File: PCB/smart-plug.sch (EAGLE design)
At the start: 10 parts, among them K1 HLS8L-DC3V-S-C, T1 2N2222

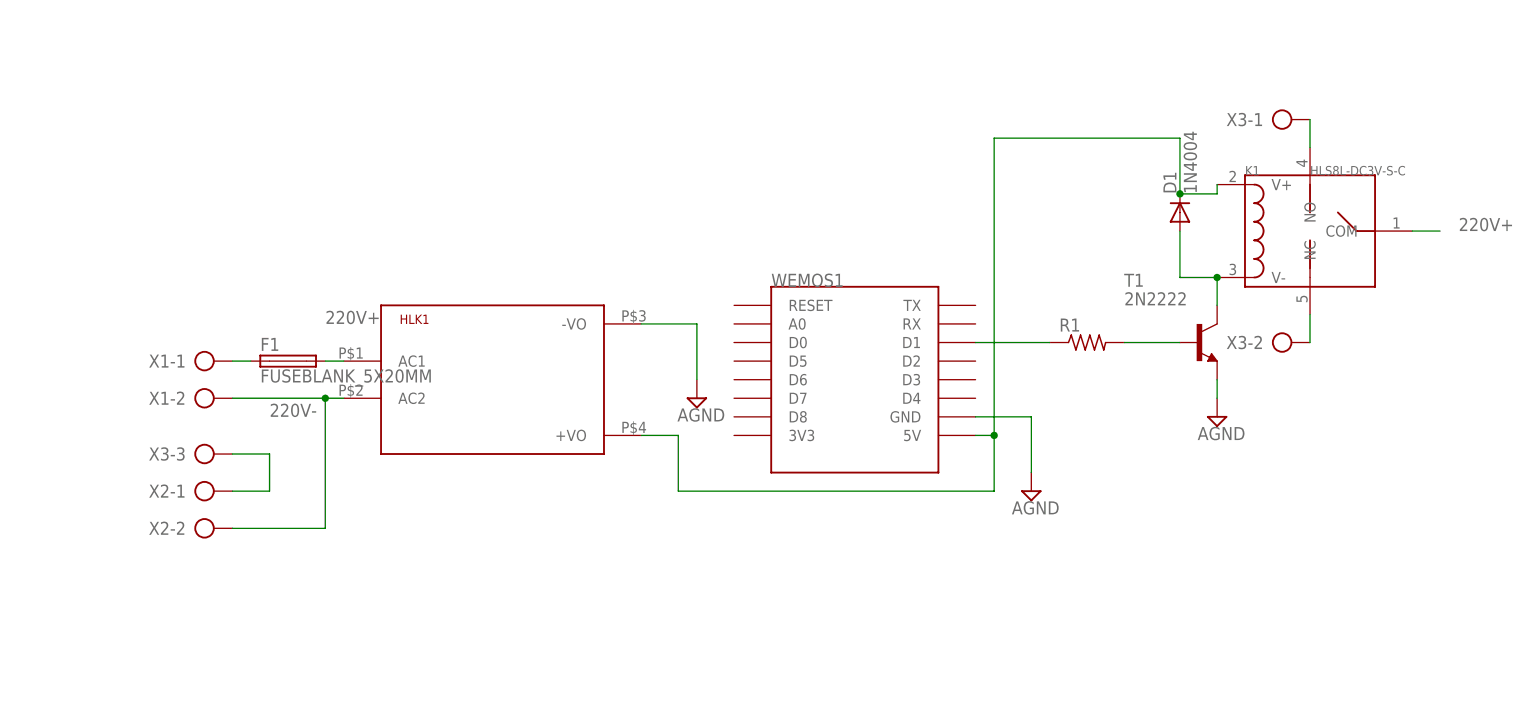
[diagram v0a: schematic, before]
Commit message: Update files
Added LED indicators
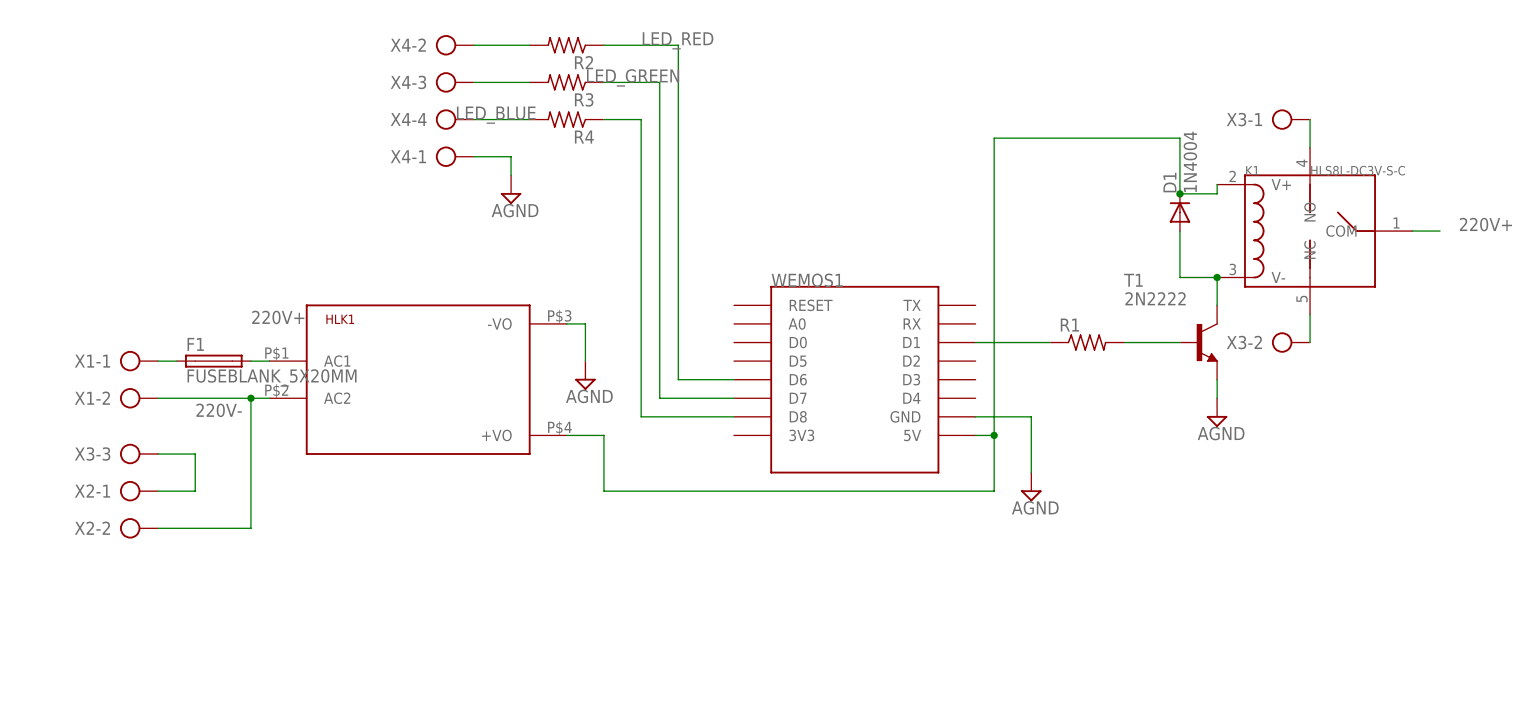
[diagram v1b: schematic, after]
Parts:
- added R2, R3, R4: (no value), adafruit:R-US_0207/10
- added X4: (no value), con-ptr500:AK300/4
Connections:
- new net LED_BLUE: R4.1, WEMOS1.D8
- new net LED_GREEN: R3.1, WEMOS1.D7
- new net LED_RED: R2.1, WEMOS1.D6
- new net N$10: R4.2, X4-4.KL
- new net N$11: R3.2, X4-3.KL
- new net N$9: R2.2, X4-2.KL
- net AGND: now also X4-1.KL
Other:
- moved on the sheet: F1, HLK1, X1-1, X1-2, X2-1, X2-2, X3-3
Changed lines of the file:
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@@
 <part name="F1" library="fuse" library_urn="urn:adsk.eagle:library:233" deviceset="FUSE" device="BLANK_5X20MM" package3d_urn="urn:adsk.eagle:package:14079/1"/>
 <part name="SUPPLY3" library="supply2" library_urn="urn:adsk.eagle:library:372" deviceset="AGND" device=""/>
+<part name="R2" library="adafruit" deviceset="R-US_" device="0207/10"/>
+<part name="R3" library="adafruit" deviceset="R-US_" device="0207/10"/>
+<part name="R4" library="adafruit" deviceset="R-US_" device="0207/10"/>
+<part name="X4" library="con-ptr500" library_urn="urn:adsk.eagle:library:181" deviceset="AK300/4" device="" package3d_urn="urn:adsk.eagle:package:9879/1"/>
+<part name="SUPPLY4" library="supply2" library_urn="urn:adsk.eagle:library:372" deviceset="AGND" device=""/>
 </parts>
 <sheets>
@@
 <instance part="SUPPLY2" gate="G$1" x="142.24" y="58.42"/>
 <instance part="D1" gate="1" x="137.16" y="86.36" rot="R90"/>
-<instance part="HLK1" gate="G$1" x="43.18" y="63.5"/>
-<instance part="X1" gate="-1" x="2.54" y="66.04"/>
-<instance part="X1" gate="-2" x="2.54" y="60.96"/>
-<instance part="X2" gate="-1" x="2.54" y="48.26"/>
-<instance part="X2" gate="-2" x="2.54" y="43.18"/>
+<instance part="HLK1" gate="G$1" x="33.02" y="63.5"/>
+<instance part="X1" gate="-1" x="-7.62" y="66.04"/>
+<instance part="X1" gate="-2" x="-7.62" y="60.96"/>
+<instance part="X2" gate="-1" x="-7.62" y="48.26"/>
+<instance part="X2" gate="-2" x="-7.62" y="43.18"/>
 <instance part="X3" gate="-1" x="149.86" y="99.06"/>
 <instance part="X3" gate="-2" x="149.86" y="68.58"/>
-<instance part="X3" gate="-3" x="2.54" y="53.34"/>
-<instance part="F1" gate="G$1" x="15.24" y="66.04"/>
-<instance part="SUPPLY3" gate="G$1" x="71.12" y="60.96"/>
+<instance part="X3" gate="-3" x="-7.62" y="53.34"/>
+<instance part="F1" gate="G$1" x="5.08" y="66.04"/>
+<instance part="SUPPLY3" gate="G$1" x="55.88" y="63.5"/>
+<instance part="R2" gate="G$1" x="53.34" y="109.22" rot="R180"/>
+<instance part="R3" gate="G$1" x="53.34" y="104.14" rot="R180"/>
+<instance part="R4" gate="G$1" x="53.34" y="99.06" rot="R180"/>
+<instance part="X4" gate="-1" x="35.56" y="93.98"/>
+<instance part="X4" gate="-2" x="35.56" y="109.22"/>
+<instance part="X4" gate="-3" x="35.56" y="104.14"/>
+<instance part="X4" gate="-4" x="35.56" y="99.06"/>
+<instance part="SUPPLY4" gate="G$1" x="45.72" y="88.9"/>
 </instances>
 <busses>
 </busses>
 <nets>
-<net name="N$2" class="0">
-<segment>
-<pinref part="WEMOS1" gate="D1" pin="D1"/>
-<pinref part="R1" gate="G$1" pin="1"/>
-<wire x1="109.22" y1="68.58" x2="119.38" y2="68.58" width="0.1524" layer="91"/>
-</segment>
-</net>
 <net name="N$3" class="0">
 <segment>
@@
 <wire x1="111.76" y1="55.88" x2="109.22" y2="55.88" width="0.1524" layer="91"/>
 <pinref part="HLK1" gate="G$1" pin="+VO"/>
-<wire x1="63.5" y1="55.88" x2="68.58" y2="55.88" width="0.1524" layer="91"/>
-<wire x1="68.58" y1="55.88" x2="68.58" y2="48.26" width="0.1524" layer="91"/>
-<wire x1="68.58" y1="48.26" x2="111.76" y2="48.26" width="0.1524" layer="91"/>
+<wire x1="53.34" y1="55.88" x2="58.42" y2="55.88" width="0.1524" layer="91"/>
+<wire x1="58.42" y1="55.88" x2="58.42" y2="48.26" width="0.1524" layer="91"/>
+<wire x1="58.42" y1="48.26" x2="111.76" y2="48.26" width="0.1524" layer="91"/>
 <wire x1="111.76" y1="48.26" x2="111.76" y2="55.88" width="0.1524" layer="91"/>
 <junction x="111.76" y="55.88"/>
@@
 <segment>
 <pinref part="SUPPLY3" gate="G$1" pin="AGND"/>
-<wire x1="71.12" y1="63.5" x2="71.12" y2="71.12" width="0.1524" layer="91"/>
-<wire x1="71.12" y1="71.12" x2="63.5" y2="71.12" width="0.1524" layer="91"/>
+<wire x1="55.88" y1="66.04" x2="55.88" y2="71.12" width="0.1524" layer="91"/>
+<wire x1="55.88" y1="71.12" x2="53.34" y2="71.12" width="0.1524" layer="91"/>
 <pinref part="HLK1" gate="G$1" pin="-VO"/>
+</segment>
+<segment>
+<pinref part="X4" gate="-1" pin="KL"/>
+<wire x1="40.64" y1="93.98" x2="45.72" y2="93.98" width="0.1524" layer="91"/>
+<pinref part="SUPPLY4" gate="G$1" pin="AGND"/>
+<wire x1="45.72" y1="93.98" x2="45.72" y2="91.44" width="0.1524" layer="91"/>
 </segment>
 </net>
@@
 <pinref part="F1" gate="G$1" pin="2"/>
 <pinref part="HLK1" gate="G$1" pin="AC1"/>
-<wire x1="20.32" y1="66.04" x2="22.86" y2="66.04" width="0.1524" layer="91"/>
-<label x="20.32" y="71.12" size="1.778" layer="95"/>
+<wire x1="10.16" y1="66.04" x2="12.7" y2="66.04" width="0.1524" layer="91"/>
+<label x="10.16" y="71.12" size="1.778" layer="95"/>
 </segment>
 </net>
@@
 <pinref part="X1" gate="-2" pin="KL"/>
 <pinref part="HLK1" gate="G$1" pin="AC2"/>
-<wire x1="7.62" y1="60.96" x2="20.32" y2="60.96" width="0.1524" layer="91"/>
-<label x="12.7" y="58.42" size="1.778" layer="95"/>
+<wire x1="-2.54" y1="60.96" x2="10.16" y2="60.96" width="0.1524" layer="91"/>
+<label x="2.54" y="58.42" size="1.778" layer="95"/>
 <pinref part="X2" gate="-2" pin="KL"/>
-<wire x1="20.32" y1="60.96" x2="22.86" y2="60.96" width="0.1524" layer="91"/>
-<wire x1="7.62" y1="43.18" x2="20.32" y2="43.18" width="0.1524" layer="91"/>
-<wire x1="20.32" y1="43.18" x2="20.32" y2="60.96" width="0.1524" layer="91"/>
-<junction x="20.32" y="60.96"/>
+<wire x1="10.16" y1="60.96" x2="12.7" y2="60.96" width="0.1524" layer="91"/>
+<wire x1="-2.54" y1="43.18" x2="10.16" y2="43.18" width="0.1524" layer="91"/>
+<wire x1="10.16" y1="43.18" x2="10.16" y2="60.96" width="0.1524" layer="91"/>
+<junction x="10.16" y="60.96"/>
 </segment>
 </net>
@@
 <pinref part="X1" gate="-1" pin="KL"/>
 <pinref part="F1" gate="G$1" pin="1"/>
-<wire x1="7.62" y1="66.04" x2="10.16" y2="66.04" width="0.1524" layer="91"/>
+<wire x1="-2.54" y1="66.04" x2="0" y2="66.04" width="0.1524" layer="91"/>
 </segment>
 </net>
 <net name="N$1" class="0">
 <segment>
-<wire x1="12.7" y1="53.34" x2="12.7" y2="48.26" width="0.1524" layer="91"/>
+<wire x1="2.54" y1="53.34" x2="2.54" y2="48.26" width="0.1524" layer="91"/>
 <pinref part="X2" gate="-1" pin="KL"/>
-<wire x1="12.7" y1="48.26" x2="7.62" y2="48.26" width="0.1524" layer="91"/>
+<wire x1="2.54" y1="48.26" x2="-2.54" y2="48.26" width="0.1524" layer="91"/>
 <pinref part="X3" gate="-3" pin="KL"/>
-<wire x1="7.62" y1="53.34" x2="12.7" y2="53.34" width="0.1524" layer="91"/>
+<wire x1="-2.54" y1="53.34" x2="2.54" y2="53.34" width="0.1524" layer="91"/>
 </segment>
 </net>
@@
 </segment>
 </net>
+<net name="LED_BLUE" class="0">
+<segment>
+<pinref part="WEMOS1" gate="D1" pin="D8"/>
+<wire x1="76.2" y1="58.42" x2="63.5" y2="58.42" width="0.1524" layer="91"/>
+<wire x1="63.5" y1="58.42" x2="63.5" y2="99.06" width="0.1524" layer="91"/>
+<pinref part="R4" gate="G$1" pin="1"/>
+<wire x1="63.5" y1="99.06" x2="58.42" y2="99.06" width="0.1524" layer="91"/>
+<label x="38.1" y="99.06" size="1.778" layer="95"/>
+</segment>
+</net>
+<net name="LED_GREEN" class="0">
+<segment>
+<pinref part="WEMOS1" gate="D1" pin="D7"/>
+<wire x1="76.2" y1="60.96" x2="66.04" y2="60.96" width="0.1524" layer="91"/>
+<wire x1="66.04" y1="60.96" x2="66.04" y2="104.14" width="0.1524" layer="91"/>
+<pinref part="R3" gate="G$1" pin="1"/>
+<wire x1="66.04" y1="104.14" x2="58.42" y2="104.14" width="0.1524" layer="91"/>
+<label x="55.88" y="104.14" size="1.778" layer="95"/>
+</segment>
+</net>
+<net name="LED_RED" class="0">
+<segment>
+<pinref part="WEMOS1" gate="D1" pin="D6"/>
+<wire x1="76.2" y1="63.5" x2="68.58" y2="63.5" width="0.1524" layer="91"/>
+<wire x1="68.58" y1="63.5" x2="68.58" y2="109.22" width="0.1524" layer="91"/>
+<pinref part="R2" gate="G$1" pin="1"/>
+<wire x1="68.58" y1="109.22" x2="58.42" y2="109.22" width="0.1524" layer="91"/>
+<label x="63.5" y="109.22" size="1.778" layer="95"/>
+</segment>
+</net>
+<net name="N$2" class="0">
+<segment>
+<pinref part="WEMOS1" gate="D1" pin="D1"/>
+<pinref part="R1" gate="G$1" pin="1"/>
+<wire x1="109.22" y1="68.58" x2="119.38" y2="68.58" width="0.1524" layer="91"/>
+</segment>
+</net>
+<net name="N$11" class="0">
+<segment>
+<pinref part="X4" gate="-3" pin="KL"/>
+<pinref part="R3" gate="G$1" pin="2"/>
+<wire x1="40.64" y1="104.14" x2="48.26" y2="104.14" width="0.1524" layer="91"/>
+</segment>
+</net>
+<net name="N$9" class="0">
+<segment>
+<pinref part="X4" gate="-2" pin="KL"/>
+<pinref part="R2" gate="G$1" pin="2"/>
+<wire x1="40.64" y1="109.22" x2="48.26" y2="109.22" width="0.1524" layer="91"/>
+</segment>
+</net>
+<net name="N$10" class="0">
+<segment>
+<pinref part="X4" gate="-4" pin="KL"/>
+<pinref part="R4" gate="G$1" pin="2"/>
+<wire x1="40.64" y1="99.06" x2="48.26" y2="99.06" width="0.1524" layer="91"/>
+</segment>
+</net>

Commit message: Update files
Added on board LEDs, updated design
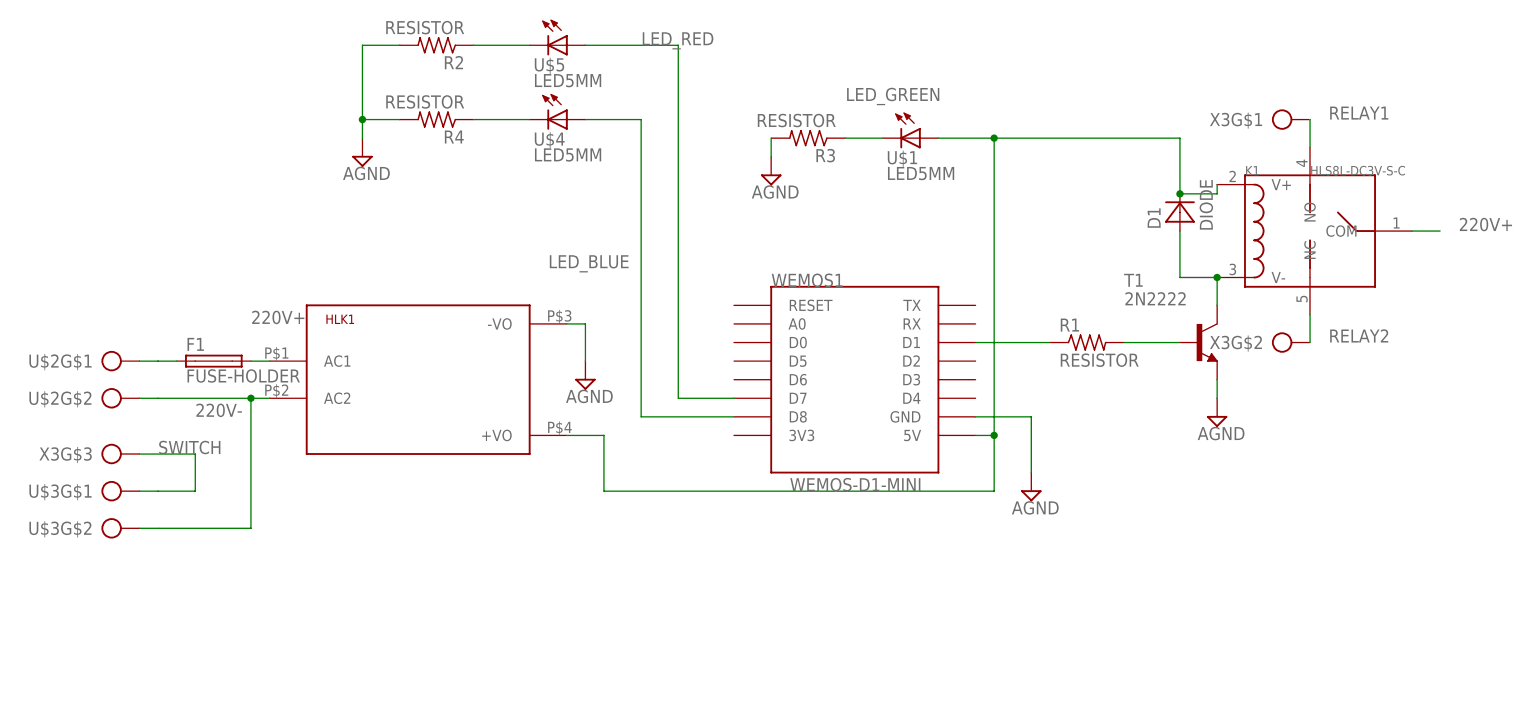
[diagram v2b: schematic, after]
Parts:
- removed X1, X2: (no value), con-ptr500:AK300/2
- removed X4: (no value), con-ptr500:AK300/4
- added U$1, U$4, U$5: LED5MM, smartplug-components:LED5MM
- added U$2, U$3: OUT-2PINS, smartplug-components:OUT-2PINS
- D1: value 1N4004 -> DIODE; device adafruit:1N4004 -> smartplug-components:DIODE
- F1: value FUSEBLANK_5X20MM -> FUSE-HOLDER; device fuse:FUSEBLANK_5X20MM -> smartplug-components:FUSE-HOLDER
- HLK1: value HLK-PM013W -> HLK-SUPPLY; device HLK-PM01:HLK-PM013W -> smartplug-components:HLK-SUPPLY
- K1: device Seeed-Relay:RELAY-HLS8L-DC3V-S-C(5P-19X15MM) -> smartplug-components:RELAY
- R1, R2, R3, R4: value (none) -> RESISTOR; device adafruit:R-US_0207/10 -> smartplug-components:RESISTOR
- WEMOS1: value (none) -> WEMOS-D1-MINI; device esp8266modules:WEMOS-D1-MINI -> smartplug-components:WEMOS-D1-MINI
- X3: value (none) -> OUT-3PINS; device con-ptr500:AK300/3 -> smartplug-components:OUT-3PINS
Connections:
- removed net N$1: X2-1.KL, X3-3.KL
- removed net N$11: R3.2, X4-3.KL
- removed net N$5: K1.NC, X3-2.KL
- removed net N$7: K1.NO, X3-1.KL
- new net RELAY1: K1.NO, X3G$1.KL
- new net RELAY2: K1.NC, X3G$2.KL
- new net SWITCH: U$3G$1.KL, X3G$3.KL
- net 220V-: now also U$2G$2.KL, U$3G$2.KL; no longer X1-2.KL, X2-2.KL
- net AGND: now also R2.2, R3.2, R4.2; no longer X4-1.KL
- net LED_BLUE: now also U$4.A; no longer R4.1
- net LED_GREEN: now also U$1.C; no longer WEMOS1.D7
- net LED_RED: now also U$5.A, WEMOS1.D7; no longer R2.1, WEMOS1.D6
- net N$10: now also R4.1, U$4.C; no longer R4.2, X4-4.KL
- net N$4: now also U$1.A
- net N$8: now also U$2G$1.KL; no longer X1-1.KL
- net N$9: now also R2.1, U$5.C; no longer R2.2, X4-2.KL
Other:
- moved on the sheet: R2, R3, R4

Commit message: Update files
Removed fuse and made PCB smaller
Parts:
- removed F1: FUSE-HOLDER, smartplug-components:FUSE-HOLDER
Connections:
- removed net N$8: F1.1, U$2G$1.KL
- net 220V+: now also U$2G$1.KL; no longer F1.2
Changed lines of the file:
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@@
 <part name="HLK1" library="smartplug-components" deviceset="HLK-SUPPLY" device=""/>
 <part name="X3" library="smartplug-components" deviceset="OUT-3PINS" device=""/>
-<part name="F1" library="smartplug-components" deviceset="FUSE-HOLDER" device=""/>
 <part name="SUPPLY3" library="supply2" library_urn="urn:adsk.eagle:library:372" deviceset="AGND" device=""/>
 <part name="R2" library="smartplug-components" deviceset="RESISTOR" device=""/>
@@
 <instance part="X3" gate="G$2" x="149.86" y="68.58"/>
 <instance part="X3" gate="G$3" x="-10.16" y="53.34"/>
-<instance part="F1" gate="G$1" x="5.08" y="66.04"/>
 <instance part="SUPPLY3" gate="G$1" x="55.88" y="63.5"/>
 <instance part="R2" gate="G$1" x="35.56" y="109.22" rot="R180"/>
@@
 </segment>
 <segment>
-<pinref part="F1" gate="G$1" pin="2"/>
 <pinref part="HLK1" gate="G$1" pin="AC1"/>
-<wire x1="10.16" y1="66.04" x2="12.7" y2="66.04" width="0.1524" layer="91"/>
 <label x="10.16" y="71.12" size="1.778" layer="95"/>
+<pinref part="U$2" gate="G$1" pin="KL"/>
+<wire x1="-5.08" y1="66.04" x2="12.7" y2="66.04" width="0.1524" layer="91"/>
 </segment>
 </net>
@@
 </segment>
 </net>
-<net name="N$8" class="0">
-<segment>
-<pinref part="F1" gate="G$1" pin="1"/>
-<wire x1="-2.54" y1="66.04" x2="0" y2="66.04" width="0.1524" layer="91"/>
-<pinref part="U$2" gate="G$1" pin="KL"/>
-<wire x1="-5.08" y1="66.04" x2="-2.54" y2="66.04" width="0.1524" layer="91"/>
-</segment>
-</net>
